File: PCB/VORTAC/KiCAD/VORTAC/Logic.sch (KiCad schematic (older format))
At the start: 61 parts, among them Q1 Q_PMOS_GSD, Q2 Q_NMOS_GSD, Q3 WSD4066DN, Q4 Q_NMOS_GSD, Q5 WSD4066DN, Q6 Q_PNP_BEC, Q7 Q_NPN_BEC, U1 TLV73333PDBV, U3 TPS54335ADRCR, U4 TPS54335ADRCR

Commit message: Routing WIP
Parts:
- C1: footprint Resistor_SMD:R_0603_1608Metric -> Capacitor_SMD:C_1206_3216Metric; LCSC (none) -> C89632
- C11, C6, C7, C9: value 0.1uF -> 0.1uF 50V
- C2: value 0.1uF -> 0.1uF 16V; footprint Capacitor_SMD:C_0402_1005Metric -> Capacitor_SMD:C_0603_1608Metric; LCSC (none) -> C66501
- C3, C8: LCSC C152910 -> (none)
- C4, C5: value 10uF -> 10uF 50V
- L1: renamed from 10uH1; value L -> 10uH
- L2: renamed from 10uH2; value L -> 10uH
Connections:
- net 12V renamed +12V
- net 3.3V renamed +3V3
- net 5V renamed +5V
- net DOCK_V_IN renamed DOCK_VDC
- net USBH_GATE renamed HOST_USB_GATE
- net V_IN renamed VDC
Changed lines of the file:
@@
 HOST_USB_DRAIN
 Text GLabel 9350 4250 0    50   Input ~ 0
-USBH_GATE
+HOST_USB_GATE
 Text GLabel 9350 4900 0    50   Input ~ 0
 LED_1_GATE
@@
 Text GLabel 9400 1050 0    50   Input ~ 0
 HEATER_DRAIN
-Text GLabel 9400 1650 0    50   Input ~ 0
-V_IN
 $Comp
 L Device:Q_NMOS_GSD Q4
@@
 F 0 "C1" V 9500 1650 50  0000 C CNN
 F 1 "10uF 50V" V 9750 1650 50  0000 C CNN
-F 2 "Resistor_SMD:R_0603_1608Metric" H 9650 1650 50  0001 C CNN
-F 3 "~" H 9650 1650 50  0001 C CNN
+F 2 "Capacitor_SMD:C_1206_3216Metric" H 9650 1650 50  0001 C CNN
+F 3 "https://www.lcsc.com/product-detail/Multilayer-Ceramic-Capacitors-MLCC-SMD-SMT_Samsung-Electro-Mechanics-CL31B106KBHNNNE_C89632.html" H 9650 1650 50  0001 C CNN
+F 4 "C89632" H 9650 1650 50  0001 C CNN "LCSC"
 	1    9650 1650
 	0    -1   -1   0
@@
 Connection ~ 10300 1650
 Text GLabel 4050 1000 2    50   Input ~ 0
-DOCK_V_IN
+DOCK_VDC
 Text GLabel 4050 2100 2    50   Input ~ 0
 DOCK_GND
@@
 	0    1    1    0
 $EndComp
-Text GLabel 1050 1000 0    50   Input ~ 0
-V_IN
 $Comp
 L Device:D D1
@@
 AR Path="/613DB78D/6170C67D" Ref="C?"  Part="1"
 F 0 "C2" H 10050 6100 50  0000 L CNN
-F 1 "0.1uF" H 10050 6000 50  0000 L CNN
-F 2 "Capacitor_SMD:C_0402_1005Metric" H 9950 6100 50  0001 C CNN
-F 3 "~" H 9950 6100 50  0001 C CNN
+F 1 "0.1uF 16V" H 10050 6000 50  0000 L CNN
+F 2 "Capacitor_SMD:C_0603_1608Metric" H 9950 6100 50  0001 C CNN
+F 3 "https://www.lcsc.com/product-detail/Multilayer-Ceramic-Capacitors-MLCC-SMD-SMT_Samsung-Electro-Mechanics-CL10B104KO8NNNC_C66501.html" H 9950 6100 50  0001 C CNN
+F 4 "C66501" H 9950 6100 50  0001 C CNN "LCSC"
 	1    9950 6100
 	1    0    0    -1
@@
 AR Path="/613DC005/63288FE5" Ref="C?"  Part="1"
 F 0 "C9" H 2850 2700 50  0000 C CNN
-F 1 "0.1uF" H 2850 2800 50  0000 C CNN
+F 1 "0.1uF 50V" H 2850 2800 50  0000 C CNN
 F 2 "Capacitor_SMD:C_0603_1608Metric" H 3050 2750 50  0001 C CNN
 F 3 "https://www.lcsc.com/product-detail/Multilayer-Ceramic-Capacitors-MLCC-SMD-SMT_Samsung-Electro-Mechanics-CL10B104KB8NNNC_C1591.html" H 3050 2750 50  0001 C CNN
@@
 Wire Wire Line
 	2150 3100 2200 3100
-Text GLabel 1150 2950 0    50   Input ~ 0
-V_IN
 $Comp
 L Device:C_Small C4
@@
 AR Path="/613DC005/63289031" Ref="C?"  Part="1"
 F 0 "C4" H 1300 3100 50  0000 C CNN
-F 1 "10uF" H 1300 3200 50  0000 C CNN
+F 1 "10uF 50V" H 1300 3200 50  0000 C CNN
 F 2 "Capacitor_SMD:C_1206_3216Metric" H 1450 3150 50  0001 C CNN
 F 3 "https://www.lcsc.com/product-detail/Multilayer-Ceramic-Capacitors-MLCC-SMD-SMT_Samsung-Electro-Mechanics-CL31B106KBHNNNE_C89632.html" H 1450 3150 50  0001 C CNN
@@
 AR Path="/613DC005/63289038" Ref="C?"  Part="1"
 F 0 "C6" H 1650 3100 50  0000 C CNN
-F 1 "0.1uF" H 1650 3200 50  0000 C CNN
+F 1 "0.1uF 50V" H 1650 3200 50  0000 C CNN
 F 2 "Capacitor_SMD:C_0603_1608Metric" H 1800 3150 50  0001 C CNN
 F 3 "https://www.lcsc.com/product-detail/Multilayer-Ceramic-Capacitors-MLCC-SMD-SMT_Samsung-Electro-Mechanics-CL10B104KB8NNNC_C1591.html" H 1800 3150 50  0001 C CNN
@@
 AR Path="/613DC005/63289050" Ref="C?"  Part="1"
 F 0 "C11" H 2850 4700 50  0000 C CNN
-F 1 "0.1uF" H 2850 4800 50  0000 C CNN
+F 1 "0.1uF 50V" H 2850 4800 50  0000 C CNN
 F 2 "Capacitor_SMD:C_0603_1608Metric" H 3050 4750 50  0001 C CNN
 F 3 "https://www.lcsc.com/product-detail/Multilayer-Ceramic-Capacitors-MLCC-SMD-SMT_Samsung-Electro-Mechanics-CL10B104KB8NNNC_C1591.html" H 3050 4750 50  0001 C CNN
@@
 P 3250 4600
 AR Path="/613DC005/6328905D" Ref="10uH?"  Part="1"
-AR Path="/613DBE83/6328905D" Ref="10uH2"  Part="1"
-F 0 "10uH2" V 3200 4600 50  0000 C CNN
-F 1 "L" V 3350 4600 50  0000 C CNN
+AR Path="/613DBE83/6328905D" Ref="L2"  Part="1"
+F 0 "L2" V 3200 4600 50  0000 C CNN
+F 1 "10uH" V 3350 4600 50  0000 C CNN
 F 2 "ToolChanger:L_Sunlord_MWSA0518_5.4x5.2mm" H 3250 4600 50  0001 C CNN
 F 3 "https://www.lcsc.com/product-detail/Power-Inductors_Sunlord-MWSA0503S-100MT_C408412.html" H 3250 4600 50  0001 C CNN
@@
 Wire Wire Line
 	3050 5900 3350 5900
-Text GLabel 4500 4600 2    50   Input ~ 0
-5V
 Wire Wire Line
 	4350 4600 4500 4600
@@
 Wire Wire Line
 	2150 5100 2200 5100
-Text GLabel 1150 4950 0    50   Input ~ 0
-V_IN
 $Comp
 L Device:C_Small C5
@@
 AR Path="/613DC005/632890DF" Ref="C?"  Part="1"
 F 0 "C5" H 1300 5100 50  0000 C CNN
-F 1 "10uF" H 1300 5200 50  0000 C CNN
+F 1 "10uF 50V" H 1300 5200 50  0000 C CNN
 F 2 "Capacitor_SMD:C_1206_3216Metric" H 1450 5150 50  0001 C CNN
 F 3 "https://www.lcsc.com/product-detail/Multilayer-Ceramic-Capacitors-MLCC-SMD-SMT_Samsung-Electro-Mechanics-CL31B106KBHNNNE_C89632.html" H 1450 5150 50  0001 C CNN
@@
 AR Path="/613DC005/632890E6" Ref="C?"  Part="1"
 F 0 "C7" H 1650 5100 50  0000 C CNN
-F 1 "0.1uF" H 1650 5200 50  0000 C CNN
+F 1 "0.1uF 50V" H 1650 5200 50  0000 C CNN
 F 2 "Capacitor_SMD:C_0603_1608Metric" H 1800 5150 50  0001 C CNN
 F 3 "https://www.lcsc.com/product-detail/Multilayer-Ceramic-Capacitors-MLCC-SMD-SMT_Samsung-Electro-Mechanics-CL10B104KB8NNNC_C1591.html" H 1800 5150 50  0001 C CNN
@@
 Wire Wire Line
 	4350 2600 4500 2600
-Text GLabel 4500 2600 2    50   Input ~ 0
-12V
 Connection ~ 3750 2950
 Wire Wire Line
@@
 P 3250 2600
 AR Path="/613DC005/6328913B" Ref="10uH?"  Part="1"
-AR Path="/613DBE83/6328913B" Ref="10uH1"  Part="1"
-F 0 "10uH1" V 3200 2600 50  0000 C CNN
-F 1 "L" V 3350 2600 50  0000 C CNN
+AR Path="/613DBE83/6328913B" Ref="L1"  Part="1"
+F 0 "L1" V 3200 2600 50  0000 C CNN
+F 1 "10uH" V 3350 2600 50  0000 C CNN
 F 2 "ToolChanger:L_Sunlord_MWSA0518_5.4x5.2mm" H 3250 2600 50  0001 C CNN
 F 3 "https://www.lcsc.com/product-detail/Power-Inductors_Sunlord-MWSA0503S-100MT_C408412.html" H 3250 2600 50  0001 C CNN
@@
 	1    0    0    -1
 $EndComp
-Text GLabel 1050 6900 0    50   Input ~ 0
-5V
-Text GLabel 2050 6900 2    50   Input ~ 0
-3.3V
 $Comp
 L Device:C_Small C8
@@
 F 1 "1uF" H 2100 7250 50  0000 C CNN
 F 2 "Capacitor_SMD:C_0603_1608Metric" H 1950 7200 50  0001 C CNN
-F 3 "https://www.lcsc.com/product-detail/Multilayer-Ceramic-Capacitors-MLCC-SMD-SMT_Walsin-Tech-Corp-0603N332J500CT_C152910.html" H 1950 7200 50  0001 C CNN
-F 4 "C152910" H 1950 7200 50  0001 C CNN "LCSC"
+F 3 "" H 1950 7200 50  0001 C CNN
+F 4 "" H 1950 7200 50  0001 C CNN "LCSC"
 	1    1950 7200
 	1    0    0    -1
@@
 F 1 "1uF" H 1000 7250 50  0000 C CNN
 F 2 "Capacitor_SMD:C_0603_1608Metric" H 1150 7200 50  0001 C CNN
-F 3 "https://www.lcsc.com/product-detail/Multilayer-Ceramic-Capacitors-MLCC-SMD-SMT_Walsin-Tech-Corp-0603N332J500CT_C152910.html" H 1150 7200 50  0001 C CNN
-F 4 "C152910" H 1150 7200 50  0001 C CNN "LCSC"
+F 3 "" H 1150 7200 50  0001 C CNN
+F 4 "" H 1150 7200 50  0001 C CNN "LCSC"
 	1    1150 7200
 	1    0    0    -1
@@
 Wire Wire Line
 	9450 4050 10250 4050
+$Comp
+L power:VDC #PWR0140
+U 1 1 61FDF6CF
+P 9400 1650
+F 0 "#PWR0140" H 9400 1550 50  0001 C CNN
+F 1 "VDC" V 9415 1777 50  0000 L CNN
+F 2 "" H 9400 1650 50  0001 C CNN
+F 3 "" H 9400 1650 50  0001 C CNN
+	1    9400 1650
+	0    -1   -1   0
+$EndComp
+$Comp
+L power:VDC #PWR0141
+U 1 1 620077AC
+P 1050 1000
+F 0 "#PWR0141" H 1050 900 50  0001 C CNN
+F 1 "VDC" V 1065 1127 50  0000 L CNN
+F 2 "" H 1050 1000 50  0001 C CNN
+F 3 "" H 1050 1000 50  0001 C CNN
+	1    1050 1000
+	0    -1   -1   0
+$EndComp
+$Comp
+L power:VDC #PWR0142
+U 1 1 62013F8B
+P 1150 2950
+F 0 "#PWR0142" H 1150 2850 50  0001 C CNN
+F 1 "VDC" V 1165 3077 50  0000 L CNN
+F 2 "" H 1150 2950 50  0001 C CNN
+F 3 "" H 1150 2950 50  0001 C CNN
+	1    1150 2950
+	0    -1   -1   0
+$EndComp
+$Comp
+L power:VDC #PWR0143
+U 1 1 62022D6D
+P 1150 4950
+F 0 "#PWR0143" H 1150 4850 50  0001 C CNN
+F 1 "VDC" V 1150 5100 50  0000 L CNN
+F 2 "" H 1150 4950 50  0001 C CNN
+F 3 "" H 1150 4950 50  0001 C CNN
+	1    1150 4950
+	0    -1   -1   0
+$EndComp
+$Comp
+L power:+5V #PWR0144
+U 1 1 6203746B
+P 1050 6900
+F 0 "#PWR0144" H 1050 6750 50  0001 C CNN
+F 1 "+5V" V 1065 7028 50  0000 L CNN
+F 2 "" H 1050 6900 50  0001 C CNN
+F 3 "" H 1050 6900 50  0001 C CNN
+	1    1050 6900
+	0    -1   -1   0
+$EndComp
+$Comp
+L power:+3.3V #PWR0145
+U 1 1 62038159
+P 2050 6900
+F 0 "#PWR0145" H 2050 6750 50  0001 C CNN
+F 1 "+3.3V" V 2065 7028 50  0000 L CNN
+F 2 "" H 2050 6900 50  0001 C CNN
+F 3 "" H 2050 6900 50  0001 C CNN
+	1    2050 6900
+	0    1    1    0
+$EndComp
+$Comp
+L power:+5V #PWR0146
+U 1 1 6203A774
+P 4500 4600
+F 0 "#PWR0146" H 4500 4450 50  0001 C CNN
+F 1 "+5V" V 4515 4728 50  0000 L CNN
+F 2 "" H 4500 4600 50  0001 C CNN
+F 3 "" H 4500 4600 50  0001 C CNN
+	1    4500 4600
+	0    1    1    0
+$EndComp
+$Comp
+L power:+12V #PWR0147
+U 1 1 62048089
+P 4500 2600
+F 0 "#PWR0147" H 4500 2450 50  0001 C CNN
+F 1 "+12V" V 4515 2728 50  0000 L CNN
+F 2 "" H 4500 2600 50  0001 C CNN
+F 3 "" H 4500 2600 50  0001 C CNN
+	1    4500 2600
+	0    1    1    0
+$EndComp
 $EndSCHEMATC

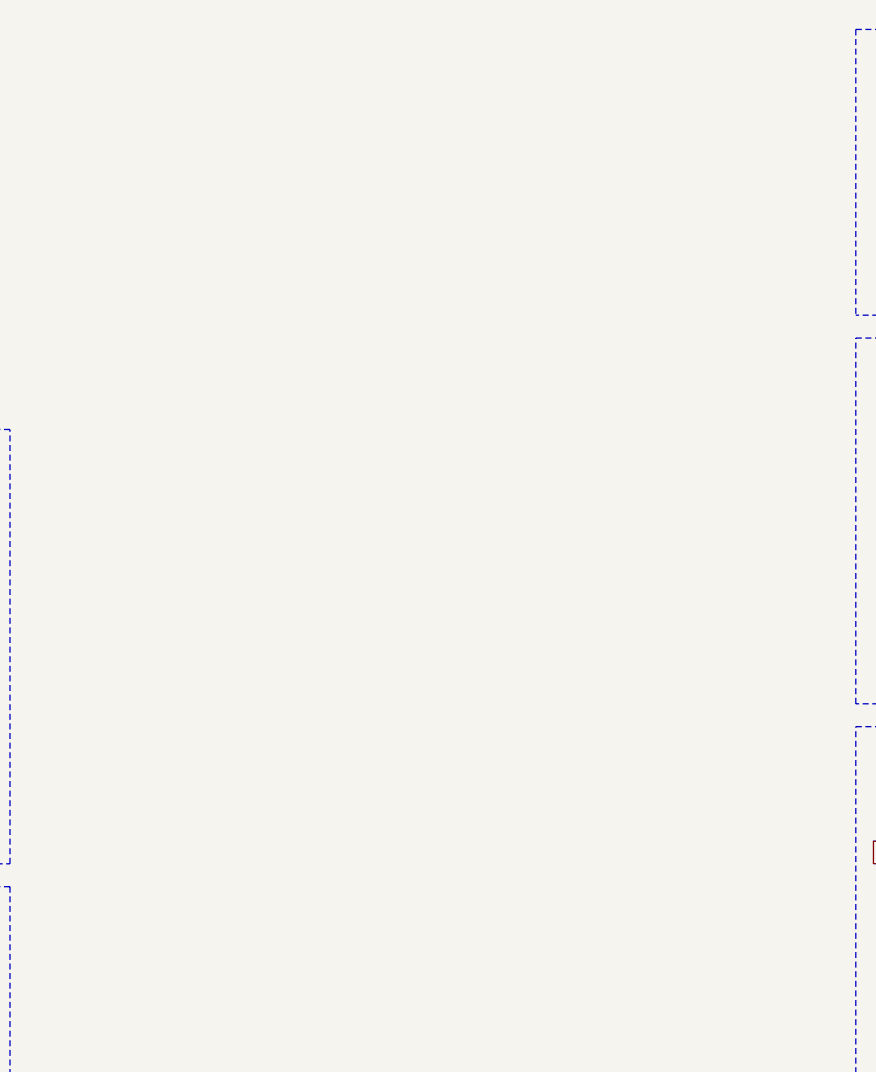
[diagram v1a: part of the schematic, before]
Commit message: Added Protective Passives
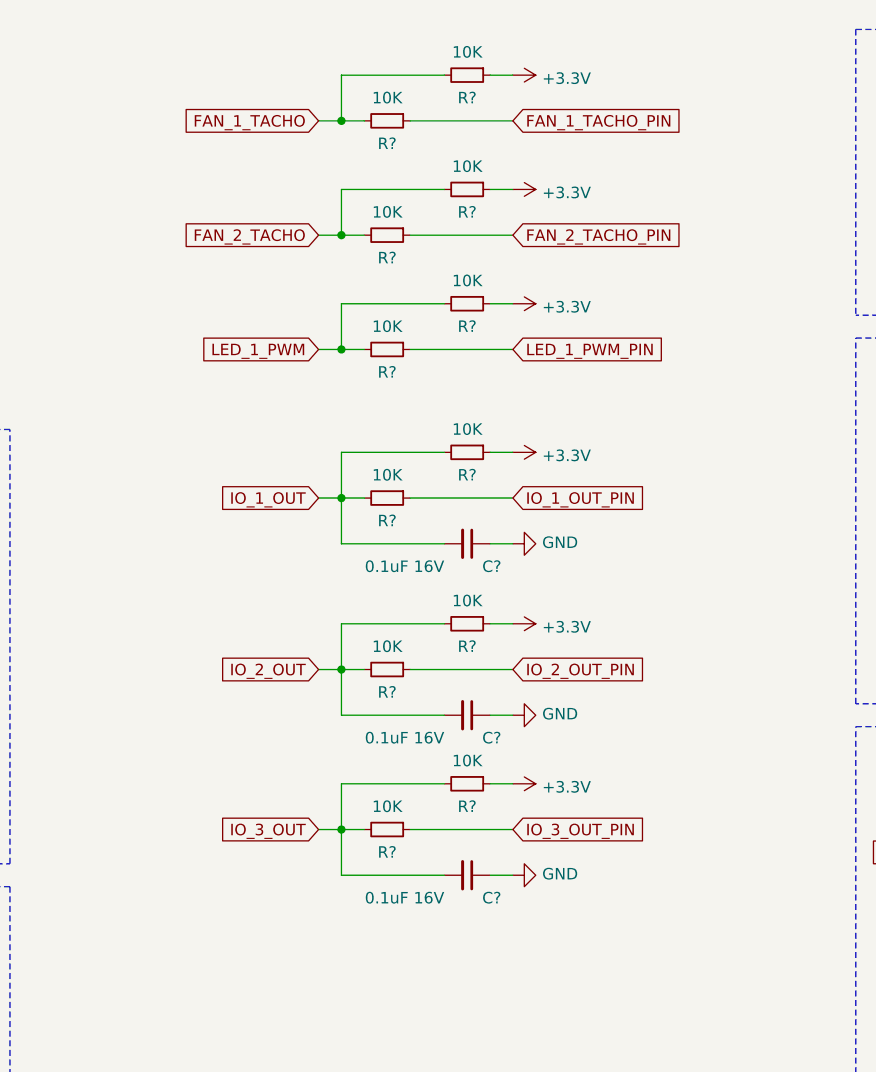
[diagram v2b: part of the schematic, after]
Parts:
- added C? (x3): 0.1uF 16V, Capacitor_SMD:C_0402_1005Metric, symbol Device:C_Small
- added R? (x12): 10K, Resistor_SMD:R_0402_1005Metric, symbol Device:R_Small
- Q1, Q2, Q4: footprint ToolChanger:IRF9310PbF-1_SO-8 -> ToolChanger:IRF9310PbF-1_SO-8_ThermalPad
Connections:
- net +3V3: now also R?.1, R?.1, R?.1, R?.1, R?.1, R?.1
- net GND: now also C?.1, C?.1, C?.1
- new net FAN_1_TACHO: R?.2, R?.2
- new net FAN_1_TACHO_PIN: R?.1
- new net FAN_2_TACHO: R?.2, R?.2
- new net FAN_2_TACHO_PIN: R?.1
- new net IO_1_OUT: C?.2, R?.2, R?.2
- new net IO_1_OUT_PIN: R?.1
- new net IO_2_OUT: C?.2, R?.2, R?.2
- new net IO_2_OUT_PIN: R?.1
- new net IO_3_OUT: C?.2, R?.2, R?.2
- new net IO_3_OUT_PIN: R?.1
- new net LED_1_PWM: R?.2, R?.2
- new net LED_1_PWM_PIN: R?.1
